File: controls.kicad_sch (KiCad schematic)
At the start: 21 parts, among them J10 CV2, J11 IN2, J12 IN 1x8h, J13 OUT1, J14 OUT2, J5 CV 1x5h, J6 OUT 1x2h, J7 LED 1x3h, J8 CV1, J9 IN1

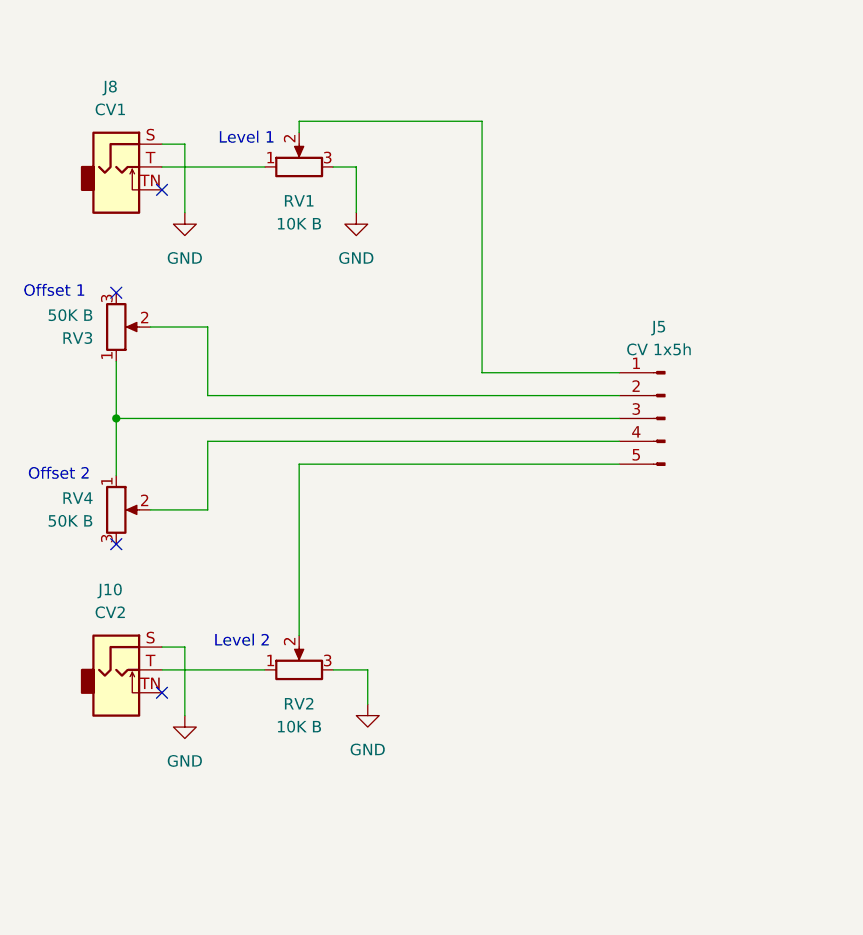
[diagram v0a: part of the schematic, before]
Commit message: Added input LED
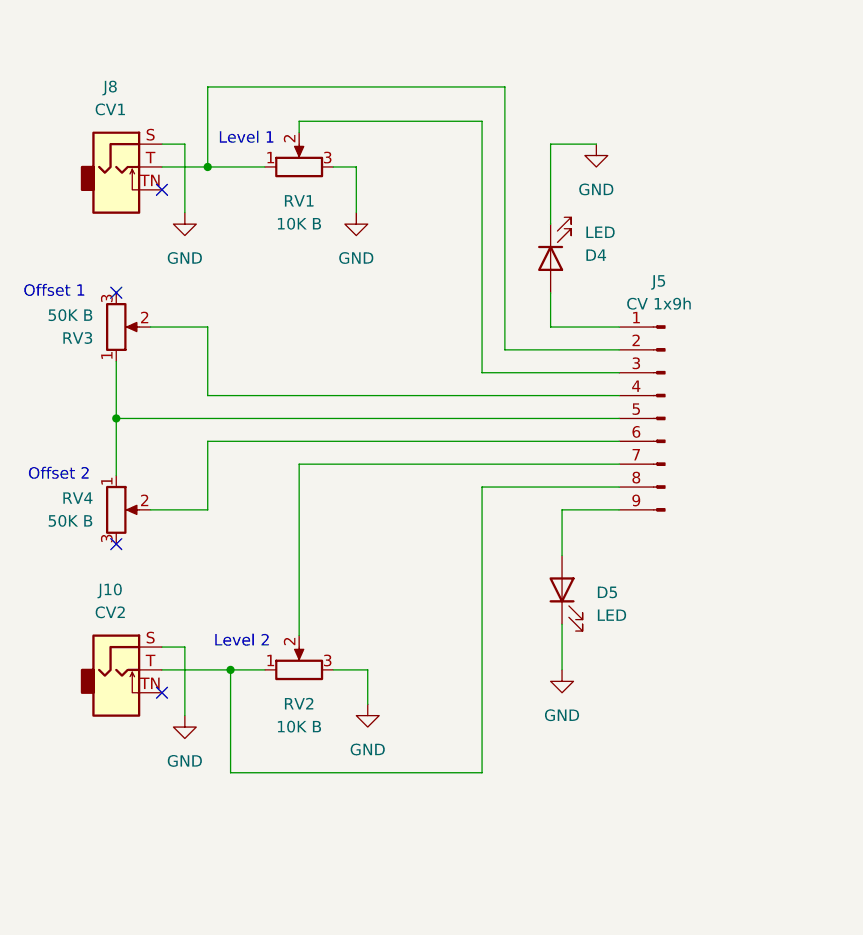
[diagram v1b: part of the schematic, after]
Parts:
- removed J5: CV 1x5h, symbol Connector:Conn_01x05_Pin
- added D4, D5: LED, LED_THT:LED_D3.0mm_FlatTop, symbol Device:LED
- added J5: CV 1x9h, symbol Connector:Conn_01x09_Pin
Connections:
- net GND: now also D4.1 (K), D5.1 (K)
- net at J10.T, RV2.1: now also J5.8 (Pin_8)
- net at RV2.2: now also J5.7 (Pin_7)
- net at J8.T, RV1.1: now also J5.2 (Pin_2)
- net at RV1.2: now also J5.3 (Pin_3)
- net at RV3.2: now also J5.4 (Pin_4)
- net at RV3.1, RV4.1: now also J5.5 (Pin_5)
- net at RV4.2: now also J5.6 (Pin_6)
- new net: D4.2 (A), J5.1 (Pin_1)
- new net: D5.2 (A), J5.9 (Pin_9)

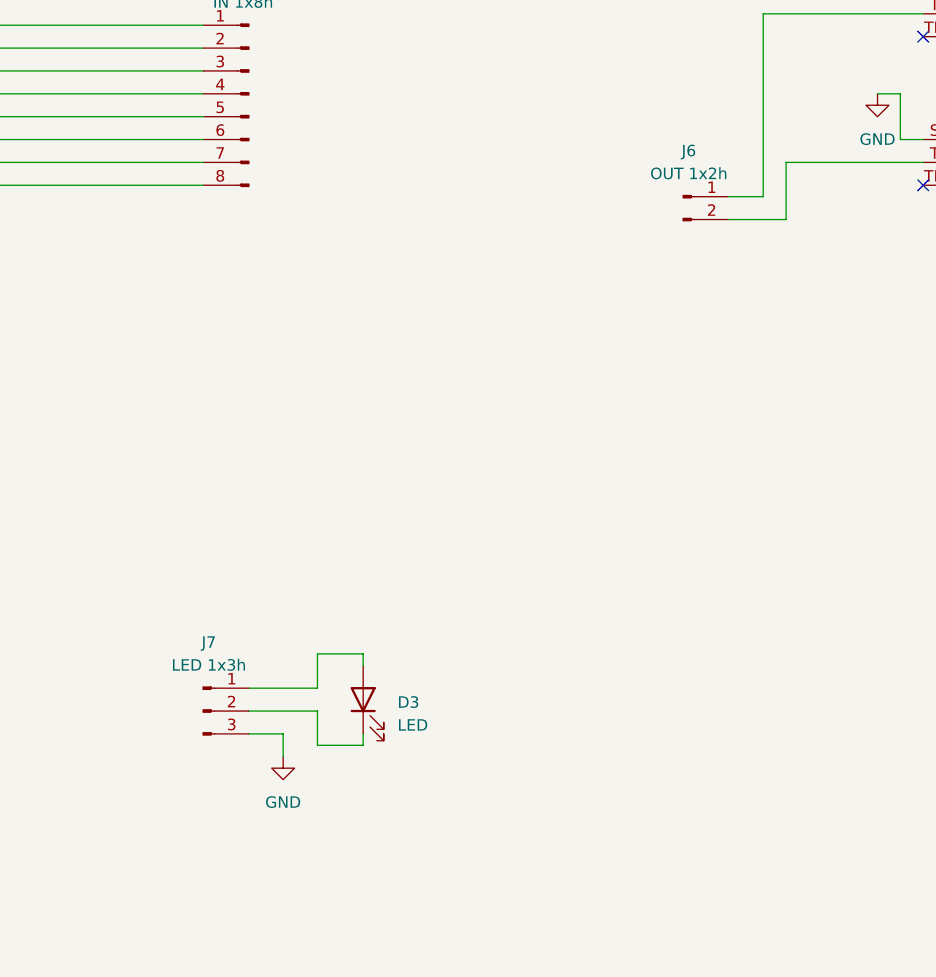
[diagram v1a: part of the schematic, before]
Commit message: Started on the PCB layout
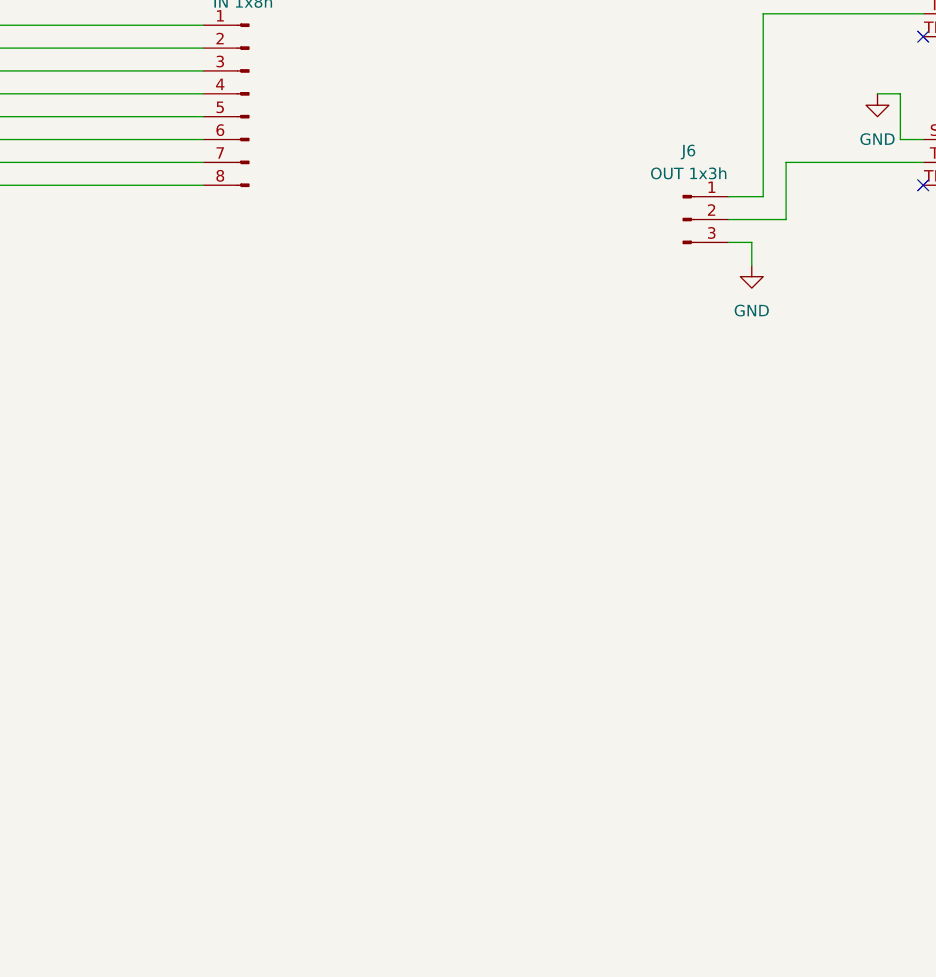
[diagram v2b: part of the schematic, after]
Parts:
- removed D3: LED, LED_THT:LED_D3.0mm_FlatTop, symbol Device:LED
- removed J6: OUT 1x2h, symbol Connector:Conn_01x02_Pin
- removed J7: LED 1x3h, symbol Connector:Conn_01x03_Pin
- added J6: OUT 1x3h, Connector_PinHeader_2.54mm:PinHeader_1x03_P2.54mm_Vertical, symbol Connector:Conn_01x03_Pin
- J12: footprint (none) -> Connector_PinHeader_2.54mm:PinHeader_1x08_P2.54mm_Vertical
- J5: footprint (none) -> Connector_PinHeader_2.54mm:PinHeader_1x09_P2.54mm_Vertical
- RV1, RV2, RV3, RV4, RV5, RV6: footprint (none) -> Potentiometer_THT:Potentiometer_Alps_RK09L_Single_Vertical
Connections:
- net GND: now also J6.3 (Pin_3)
- net at J13.T: now also J6.1 (Pin_1)
- net at J14.T: now also J6.2 (Pin_2)
